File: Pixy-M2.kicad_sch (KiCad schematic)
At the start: 71 parts, among them J1 USB_C_Receptacle_USB2.0_14P, J2 Conn_01x22_Pin, J3 Conn_01x22_Pin, J4 SM06B-SRSS-TB, J5 SM06B-SRSS-TB, J6 SM06B-SRSS-TB, J7 SM06B-SRSS-TB, J8 S6B-PH-K, J9 S6B-PH-K, Q1 AO4407A, SW1 SW_Push, SW2 SW_Push, SW3 JS102011SAQN, U1 ESP32-S3-WROOM-1-N16, U2 USBLC6-2SC6, U3 AP63203WU, U4 DRV8231ADSG, U5 DRV8231ADSG

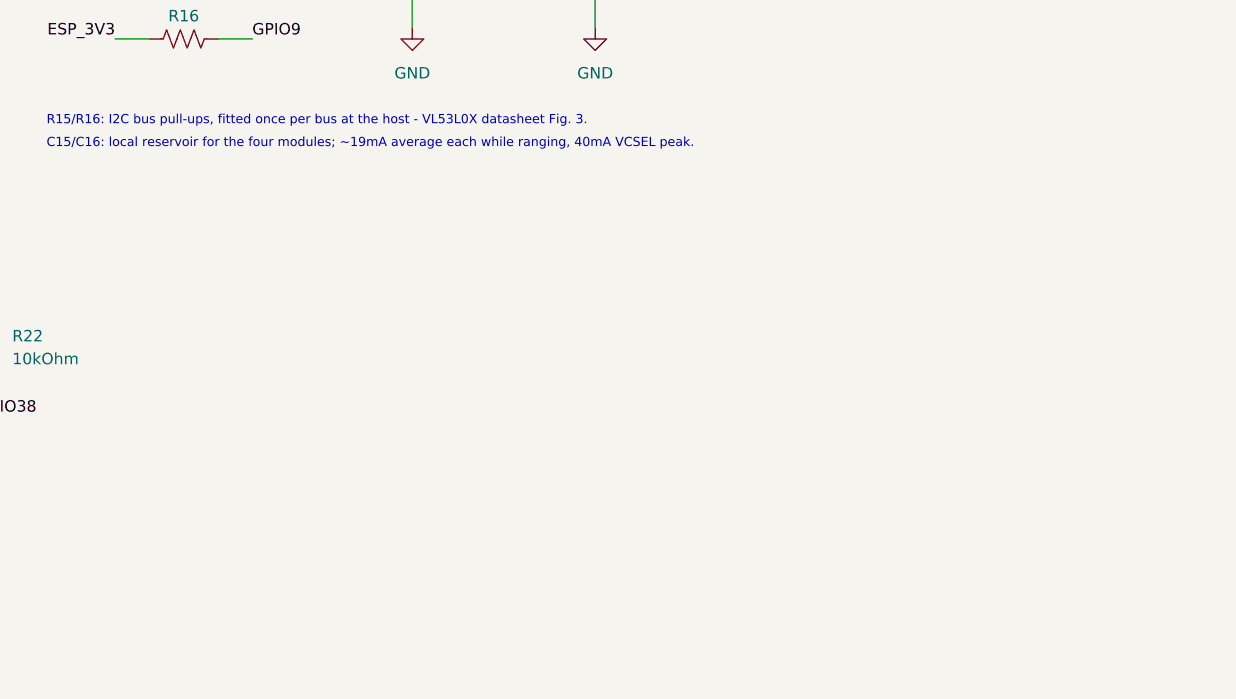
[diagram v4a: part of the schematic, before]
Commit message: Add external BNO08x IMU on SPI; drop the suction fan (issues 15, 17)
Adds J10 (SM09B-SRSS-TB, 9-pin JST-SH side-entry), R23 and C22 for an
off-board BNO08x IMU module -- the same pattern as the ToF sensors: this
board carries the connector, one pull-up and local decoupling.

Nine conductors: VIN, GND, SCK, MOSI, MISO, CS, INT, RST, WAKE. INT and
RST are not optional in SPI mode -- the part signals data-ready on INT and
the datasheet calls both required for stable SPI, which is why the
connector is 9-way rather than 6.

WAKE is pin 9 and is physically the same pin as PS0. PS0/PS1 are sampled
at reset to pick the protocol (both high = SPI), and PS0 is then repurposed
as WAKE. Hard-jumpering PS0 high would select SPI but leave the host unable
to wake a sleeping device, so WAKE goes to a GPIO and PS1 alone is the
module jumper. SparkFun's driver expects a WAK pin; Adafruit's does not.

GPIO11/12/13 are the ESP32-S3's native FSPI D/CLK/Q pins. CS is on GPIO14
because GPIO10 -- the native FSPICS0 -- is motor B's IPROPI, and CS has no
timing requirement. R23 (10k) holds RST high while GPIO16 floats at reset.
C22 is 0.1uF with no bulk cap, unlike the ToF block: C15 exists for four
VL53L0X pulsing 40mA each, while the BNO08x draws a low steady current.

Also corrects an earlier claim in this file. It said sharing the ToF I2C
bus would "cap gyro rate and couple sensor timing"; that overstated it.
Four VL53L0X at 50Hz is ~3% of a 400kHz bus and a BNO08x rotation vector at
400Hz adds ~20%, so throughput was never the issue. SPI is kept for latency
jitter -- an IMU interrupt arriving mid-ToF-read waits up to ~150us, 15% of
a 1kHz control period -- but the real costs are recorded too.

Fan: dropped from the design entirely. It was never built, so this is a
documentation change, but it improves issue 17.

F1's arithmetic is recomputed and the verdict is now "adequate, with a
thermal caveat". With no fan and the DRV8231A regulating each channel at
1.47A, the worst case the hardware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
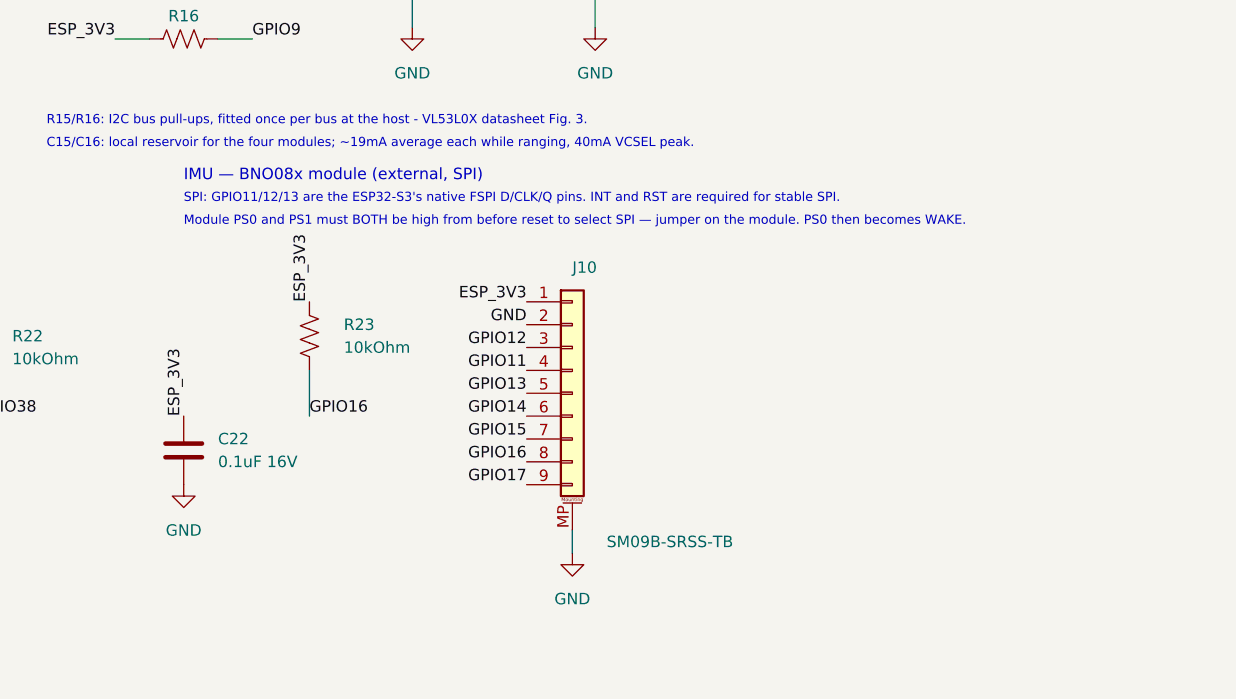
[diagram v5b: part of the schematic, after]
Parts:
- added C22: 0.1uF 16V, Capacitor_SMD:C_0603_1608Metric, symbol Device:C
- added J10: SM09B-SRSS-TB, Connector_JST:JST_SH_SM09B-SRSS-TB_1x09-1MP_P1.00mm_Horizontal, symbol Connector_Generic_MountingPin:Conn_01x09_MountingPin
- added R23: 10kOhm, Resistor_SMD:R_0805_2012Metric, symbol Device:R_US
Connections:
- net ESP_3V3: now also C22.1, J10.1 (Pin_1), R23.1
- net GND: now also C22.2, J10.2 (Pin_2), J10.MP (MountPin)
- net GPIO11: now also J10.4 (Pin_4)
- net GPIO12: now also J10.3 (Pin_3)
- net GPIO13: now also J10.5 (Pin_5)
- net GPIO14: now also J10.6 (Pin_6)
- net GPIO15: now also J10.7 (Pin_7)
- net GPIO16: now also J10.8 (Pin_8), R23.2
- net GPIO17: now also J10.9 (Pin_9)
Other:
- note added: "IMU — BNO08x module (external, SPI)"
- note added: "Module PS0 and PS1 must BOTH be high from before reset to select SPI — jumper on the module. PS0 then becomes WAKE."
- note added: "SPI: GPIO11/12/13 are the ESP32-S3's native FSPI D/CLK/Q pins. INT and RST are required for stable SPI."

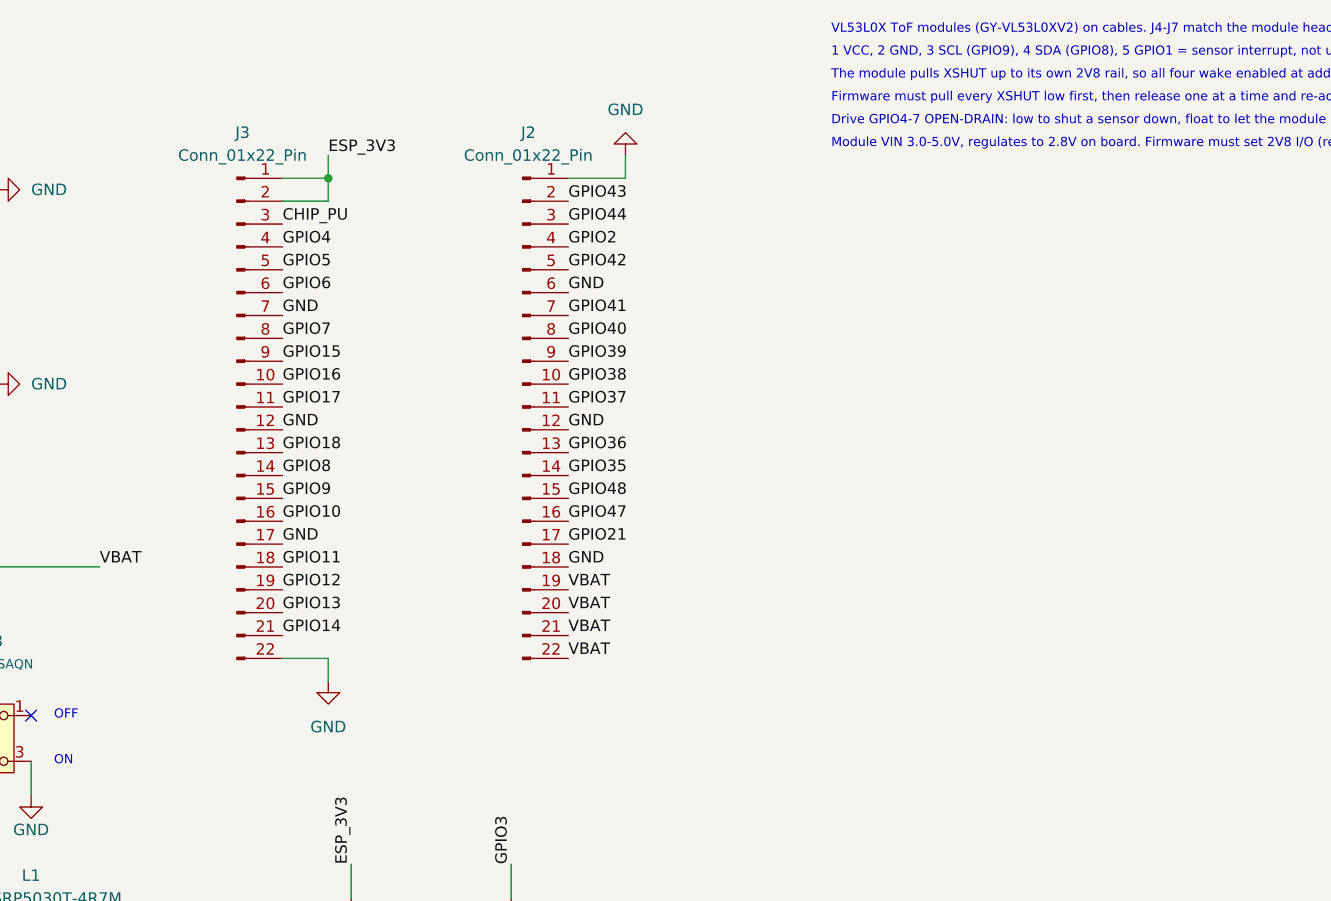
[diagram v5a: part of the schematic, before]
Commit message: Delete J2/J3; add debug header J11 and spare-GPIO pads TP5-TP9 (issue 15)
Removes the two 22-pin daughterboard headers and replaces them with a
6-pin debug header and five test pads. J2/J3 were the de-facto debug
header -- 44 pins carrying every spare GPIO -- but once the motor, IMU and
console blocks claimed those signals they carried nothing unique, while
remaining the heaviest and tallest parts on the board after the module.
Deleting them is a mass and CG win, which is what a micromouse trades on.

The precondition was that every GPIO they carried already terminates on a
real part, and that is why the deletion strands nothing. GPIO43/44 and
CHIP_PU move to J11; GPIO18/35/36/37 move to test pads; everything else
already went to the motor drivers, encoder connectors or the IMU.

J11 is SM06B-SRSS-TB, the same part as J4-J7, so it adds no BOM line and no
new cable design: 1=3V3 2=GND 3=U0TXD 4=U0RXD 5=BOOT 6=EN, mounting pegs to
GND. Pins 3-6 are an esptool auto-reset interface, and that is the
justification -- it is the recovery path if firmware ever disables the
native USB-Serial-JTAG, or if you need a console while debugging the USB
stack itself. GPIO0 was previously on no connector at all, only SW2, so
before J11 there was no off-board way into the bootloader.

JTAG deliberately gets no header. U1.13/14 are GPIO19/20 (USB D-/D+) and
already reach the USB-C port, so the ESP32-S3's built-in USB-Serial-JTAG
already provides flashing, console and JTAG over the existing connector.

TP5-TP8 carry the four spare GPIOs on TestPoint_Pad_D1.5mm, the same part
as TP1-TP4, with TP9 as a dedicated probe ground beside them -- a spare
pad with no nearby return is not much use to a logic analyser. Pads rather
than connector pins because these are bring-up aids touched with a probe,
and four 1.5mm pads weigh essentially nothing.

GPIO35/36/37 sitting on pads sharpens issue 11: on an -R8 module those
three become octal PSRAM signals, so probing them would be actively
harmful rath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
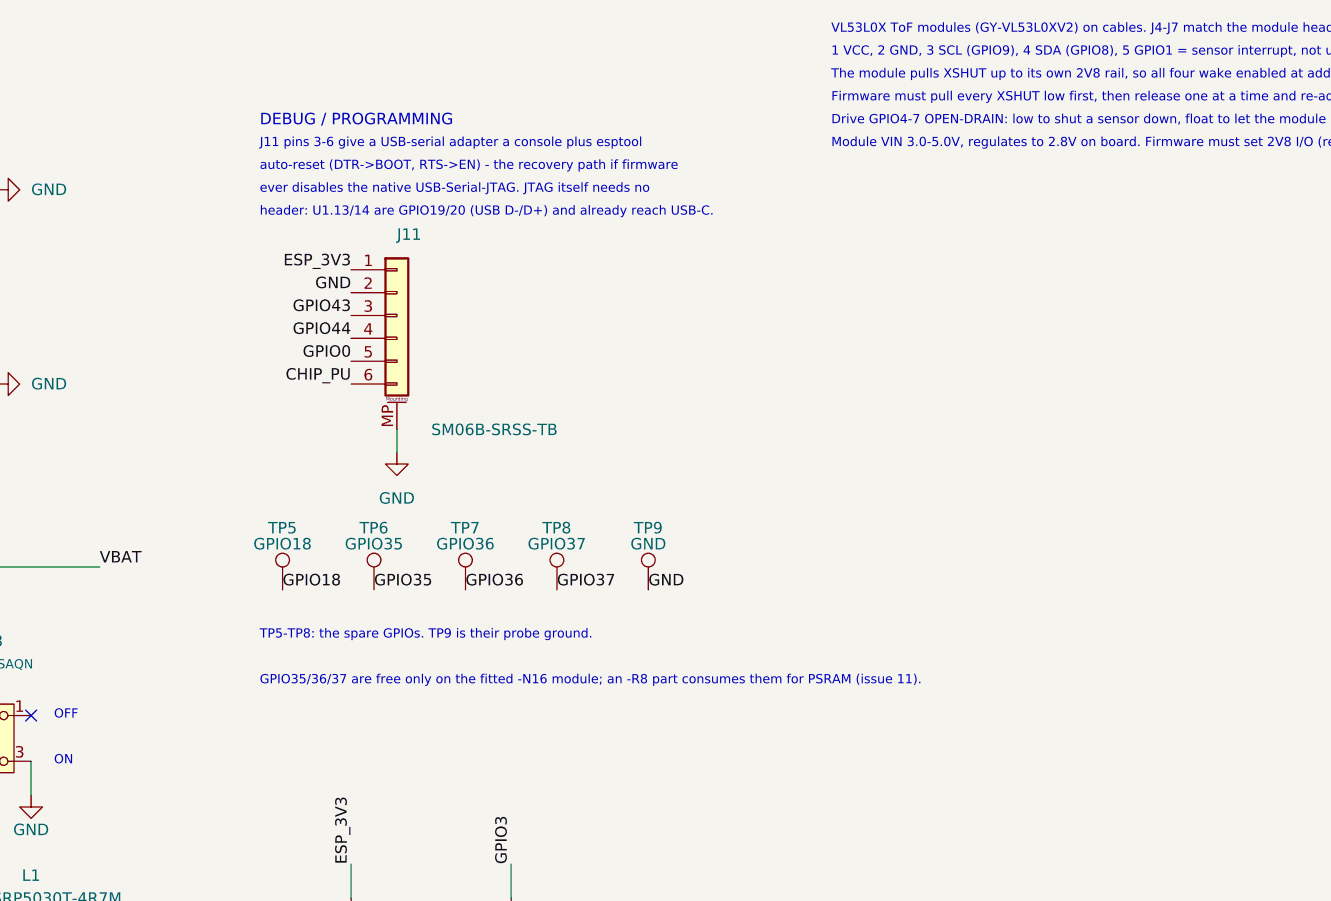
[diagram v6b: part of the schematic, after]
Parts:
- removed J2, J3: Conn_01x22_Pin, Connector_PinSocket_2.54mm:PinSocket_1x22_P2.54mm_Vertical, symbol Connector:Conn_01x22_Pin
- added J11: SM06B-SRSS-TB, Connector_JST:JST_SH_SM06B-SRSS-TB_1x06-1MP_P1.00mm_Horizontal, symbol Connector_Generic_MountingPin:Conn_01x06_MountingPin
- added TP5: GPIO18, TestPoint:TestPoint_Pad_D1.5mm, symbol Connector:TestPoint
- added TP6: GPIO35, TestPoint:TestPoint_Pad_D1.5mm, symbol Connector:TestPoint
- added TP7: GPIO36, TestPoint:TestPoint_Pad_D1.5mm, symbol Connector:TestPoint
- added TP8: GPIO37, TestPoint:TestPoint_Pad_D1.5mm, symbol Connector:TestPoint
- added TP9: GND, TestPoint:TestPoint_Pad_D1.5mm, symbol Connector:TestPoint
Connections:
- net CHIP_PU: now also J11.6 (Pin_6)
- net ESP_3V3: now also J11.1 (Pin_1)
- net GND: now also J11.2 (Pin_2), J11.MP (MountPin), TP9.1
- net GPIO0: now also J11.5 (Pin_5)
- net GPIO18: now also TP5.1
- net GPIO35: now also TP6.1
- net GPIO36: now also TP7.1
- net GPIO37: now also TP8.1
- net GPIO43: now also J11.3 (Pin_3)
- net GPIO44: now also J11.4 (Pin_4)
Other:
- note added: "DEBUG / PROGRAMMING"
- note added: "GPIO35/36/37 are free only on the fitted -N16 module; an -R8 part consumes them for PSRAM (issue 11)."
- note added: "J11 pins 3-6 give a USB-serial adapter a console plus esptool"
- note added: "TP5-TP8: the spare GPIOs. TP9 is their probe ground."
- note added: "auto-reset (DTR->BOOT, RTS->EN) - the recovery path if firmware"
- note added: "ever disables the native USB-Serial-JTAG. JTAG itself needs no"
- note added: "header: U1.13/14 are GPIO19/20 (USB D-/D+) and already reach USB-C."

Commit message: layout: clear the J1 hole-clearance errors and the U1 footprint warning
The five DRC items carried since placement are resolved without changing any
copper, footprint geometry or placement. DRC: 0 violations, 0 unconnected,
0 schematic parity issues. ERC stays 0.

J1: the stock Amphenol 12401948E412A footprint puts its GND pads 0.25 mm from
its own 0.6 mm locating holes - the land pattern KiCad's librarians merged
against Amphenol drawing c12401948 (kicad-footprints MR !3540). JLCPCB states
0.20 mm NPTH-to-track. The land pattern stays. Board-setup hole clearance is
absolute (custom rules cannot relax it), so it goes 0.30 -> 0.20 mm and a new
"Hole clearance" rule restores 0.30 mm for every pair except J1's own pads
against J1's own holes. Tested both ways: a track 0.25 mm from an SW3 hole
still fails at 0.30 mm; J1's hole moved to 0.15 mm fails the 0.20 mm floor.
CLAUDE.md wrongly named the unused USB_C_Receptacle_Amazon footprint; fixed.

U1: the board copy differed from PCM_Espressif:ESP32-S3-WROOM-1 in five items,
the antenna outline and label moved from F.SilkS to F.Fab because the antenna
overhangs the board edge. That intentional variant is now a real footprint,
Pixy-M2.pretty/ESP32-S3-WROOM-1_AntennaOverhang (Espressif's file with only
those five layer changes), registered in a project fp-lib-table. U1 points at
it in the board and in the schematic's placed instance; the cached library
symbol is left as Espressif's, since editing it raises lib_symbol_mismatch.
rework.py sets the same id via the new Pcb.set_fpid; a replay reproduces the
committed tracks and vias exactly. The board file was edited in one line
rather than regenerated, to avoid UUID churn.

Evidence: layout/drc-clean/.

Co-Authored-By: Claude Opus 5.5 <noreply@anthropic.com>
Claude-Session: https://claude.ai/code/session_01MLrob72MX5PcwtzVMbc3bs
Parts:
- U1: footprint PCM_Espressif:ESP32-S3-WROOM-1 -> Pixy-M2:ESP32-S3-WROOM-1_AntennaOverhang
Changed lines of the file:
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@@
 			)
 		)
-		(property "Footprint" "PCM_Espressif:ESP32-S3-WROOM-1"
+		(property "Footprint" "Pixy-M2:ESP32-S3-WROOM-1_AntennaOverhang"
 			(at 83.82 129.54 0)
 			(hide yes)
